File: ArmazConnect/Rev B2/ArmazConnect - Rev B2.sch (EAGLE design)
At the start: 32 parts, among them X0 NC3FAAV2, X1 NC3FAAV2, X2 NC3FAAV2, X3 NC3FAAV2, X4 NC5FAV-SW, X5 NC5MAV-SW, X6 NC5FAV-SW, X8 87832-26

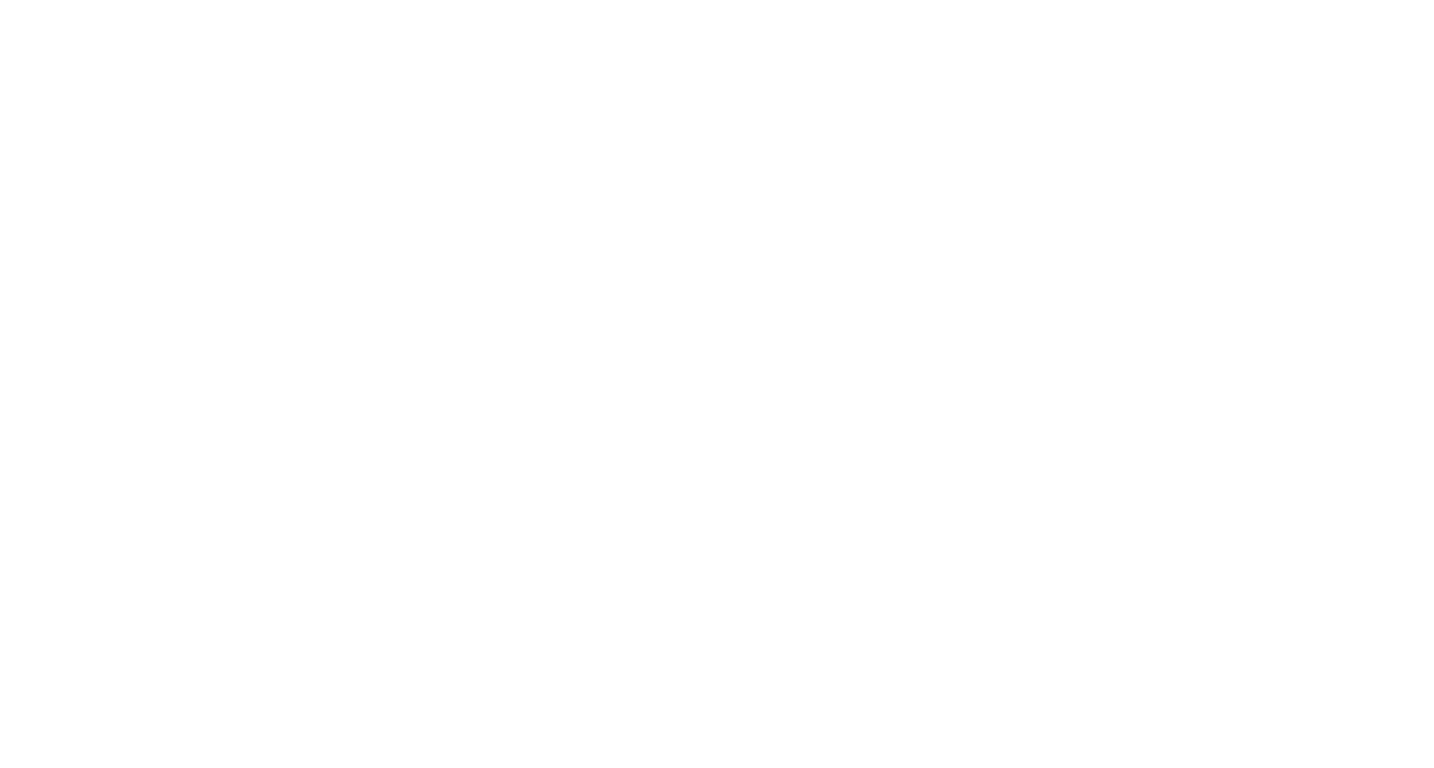
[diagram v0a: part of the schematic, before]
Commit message: Update ArmazConnect - Rev B2 schematic and board, add two dc/dc converter (12V/5V) in parallel
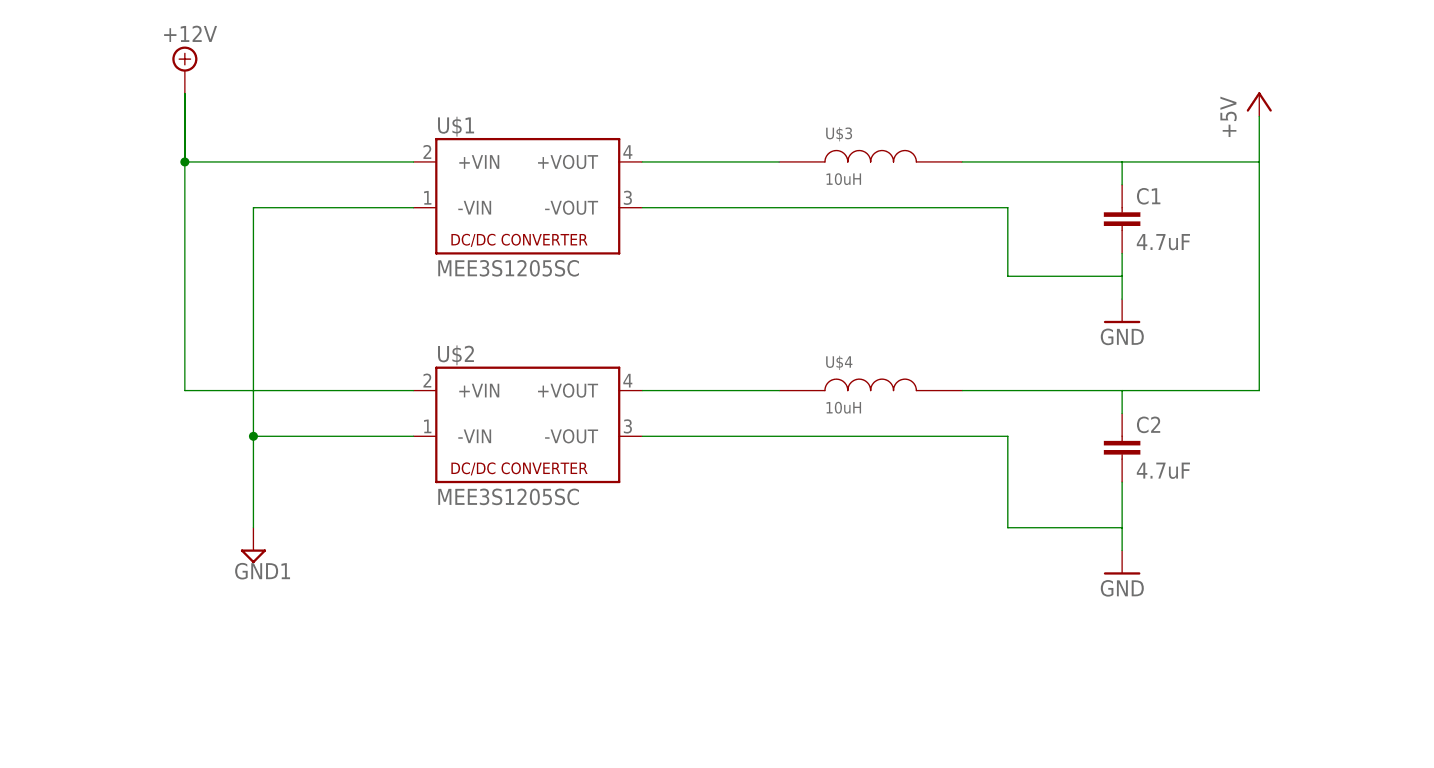
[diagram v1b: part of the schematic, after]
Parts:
- added C1, C2: 4.7uF, rcl:C-EUC0603
- added U$1, U$2: MEE3S1205SC, dc-dc-converter:MEE3S1205SC
- added U$3, U$4: 10uH, murata-inductance:84103C
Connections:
- new net N$5: U$1.+VOUT, U$3.1
- new net N$7: U$2.+VOUT, U$4.1
- net +12V: now also U$1.+VIN, U$2.+VIN
- net +5V: now also C1.1, C2.1, U$3.2, U$4.2
- net GND: now also C1.2, C2.2, U$1.-VOUT, U$2.-VOUT
- net GND1: now also U$1.-VIN, U$2.-VIN
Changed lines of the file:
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@@
 <part name="+3V2" library="supply1" deviceset="+3V3" device=""/>
 <part name="+3V3" library="supply1" deviceset="+3V3" device=""/>
+<part name="U$1" library="dc-dc-converter" deviceset="MEE3" device="" technology="S1205SC"/>
+<part name="U$2" library="dc-dc-converter" deviceset="MEE3" device="" technology="S1205SC"/>
+<part name="P+4" library="supply1" deviceset="+5V" device=""/>
+<part name="GND3" library="supply1" deviceset="GND" device=""/>
+<part name="SUPPLY4" library="supply2" deviceset="+12V" device=""/>
+<part name="SUPPLY5" library="supply2" deviceset="GND1" device=""/>
+<part name="U$3" library="murata-inductance" deviceset="84103C" device="" value="10uH"/>
+<part name="U$4" library="murata-inductance" deviceset="84103C" device="" value="10uH"/>
+<part name="C1" library="rcl" deviceset="C-EU" device="C0603" value="4.7uF"/>
+<part name="C2" library="rcl" deviceset="C-EU" device="C0603" value="4.7uF"/>
+<part name="GND4" library="supply1" deviceset="GND" device=""/>
 </parts>
 <sheets>
@@
 <instance part="+3V2" gate="G$1" x="129.54" y="144.78"/>
 <instance part="+3V3" gate="G$1" x="167.64" y="142.24"/>
+<instance part="U$1" gate="G$1" x="238.76" y="236.22"/>
+<instance part="U$2" gate="G$1" x="238.76" y="210.82"/>
+<instance part="P+4" gate="1" x="320.04" y="246.38"/>
+<instance part="GND3" gate="1" x="304.8" y="193.04" rot="MR0"/>
+<instance part="SUPPLY4" gate="+12V" x="200.66" y="248.92"/>
+<instance part="SUPPLY5" gate="G$1" x="208.28" y="195.58"/>
+<instance part="U$3" gate="L$1" x="276.86" y="238.76"/>
+<instance part="U$4" gate="L$1" x="276.86" y="213.36"/>
+<instance part="C1" gate="G$1" x="304.8" y="233.68"/>
+<instance part="C2" gate="G$1" x="304.8" y="208.28"/>
+<instance part="GND4" gate="1" x="304.8" y="220.98" rot="MR0"/>
 </instances>
 <busses>
@@
 <wire x1="167.64" y1="104.14" x2="167.64" y2="106.68" width="0.1524" layer="91"/>
 </segment>
+<segment>
+<pinref part="C1" gate="G$1" pin="2"/>
+<pinref part="GND4" gate="1" pin="GND"/>
+<wire x1="304.8" y1="223.52" x2="304.8" y2="226.06" width="0.1524" layer="91"/>
+<pinref part="U$1" gate="G$1" pin="-VOUT"/>
+<wire x1="304.8" y1="226.06" x2="304.8" y2="228.6" width="0.1524" layer="91"/>
+<wire x1="251.46" y1="233.68" x2="292.1" y2="233.68" width="0.1524" layer="91"/>
+<wire x1="292.1" y1="226.06" x2="292.1" y2="233.68" width="0.1524" layer="91"/>
+<wire x1="292.1" y1="226.06" x2="304.8" y2="226.06" width="0.1524" layer="91"/>
+</segment>
+<segment>
+<pinref part="GND3" gate="1" pin="GND"/>
+<pinref part="C2" gate="G$1" pin="2"/>
+<wire x1="304.8" y1="195.58" x2="304.8" y2="198.12" width="0.1524" layer="91"/>
+<wire x1="304.8" y1="198.12" x2="304.8" y2="203.2" width="0.1524" layer="91"/>
+<wire x1="304.8" y1="198.12" x2="292.1" y2="198.12" width="0.1524" layer="91"/>
+<wire x1="292.1" y1="198.12" x2="292.1" y2="208.28" width="0.1524" layer="91"/>
+<pinref part="U$2" gate="G$1" pin="-VOUT"/>
+<wire x1="292.1" y1="208.28" x2="251.46" y2="208.28" width="0.1524" layer="91"/>
+</segment>
 </net>
 <net name="N$27" class="0">
@@
 <wire x1="167.64" y1="116.84" x2="167.64" y2="114.3" width="0.1524" layer="91"/>
 </segment>
+<segment>
+<pinref part="U$3" gate="L$1" pin="2"/>
+<wire x1="287.02" y1="238.76" x2="304.8" y2="238.76" width="0.1524" layer="91"/>
+<pinref part="P+4" gate="1" pin="+5V"/>
+<pinref part="U$4" gate="L$1" pin="2"/>
+<wire x1="304.8" y1="238.76" x2="320.04" y2="238.76" width="0.1524" layer="91"/>
+<wire x1="320.04" y1="238.76" x2="320.04" y2="243.84" width="0.1524" layer="91"/>
+<wire x1="287.02" y1="213.36" x2="304.8" y2="213.36" width="0.1524" layer="91"/>
+<wire x1="304.8" y1="213.36" x2="320.04" y2="213.36" width="0.1524" layer="91"/>
+<wire x1="320.04" y1="213.36" x2="320.04" y2="238.76" width="0.1524" layer="91"/>
+<pinref part="C2" gate="G$1" pin="1"/>
+<wire x1="304.8" y1="210.82" x2="304.8" y2="213.36" width="0.1524" layer="91"/>
+<pinref part="C1" gate="G$1" pin="1"/>
+<wire x1="304.8" y1="236.22" x2="304.8" y2="238.76" width="0.1524" layer="91"/>
+</segment>
 </net>
 <net name="ESW0" class="0">
@@
 <junction x="30.48" y="71.12"/>
 </segment>
+<segment>
+<pinref part="U$1" gate="G$1" pin="+VIN"/>
+<pinref part="SUPPLY4" gate="+12V" pin="+12V"/>
+<wire x1="226.06" y1="238.76" x2="200.66" y2="238.76" width="0.1524" layer="91"/>
+<wire x1="200.66" y1="238.76" x2="200.66" y2="246.38" width="0.1524" layer="91"/>
+<pinref part="U$2" gate="G$1" pin="+VIN"/>
+<wire x1="200.66" y1="246.38" x2="200.66" y2="238.76" width="0.1524" layer="91"/>
+<wire x1="200.66" y1="238.76" x2="200.66" y2="213.36" width="0.1524" layer="91"/>
+<wire x1="200.66" y1="213.36" x2="226.06" y2="213.36" width="0.1524" layer="91"/>
+<junction x="200.66" y="238.76"/>
+</segment>
 </net>
 <net name="GND1" class="1">
@@
 <pinref part="SUPPLY12" gate="G$1" pin="GND1"/>
 <wire x1="167.64" y1="127" x2="167.64" y2="129.54" width="0.1524" layer="91"/>
+</segment>
+<segment>
+<pinref part="U$1" gate="G$1" pin="-VIN"/>
+<wire x1="226.06" y1="233.68" x2="208.28" y2="233.68" width="0.1524" layer="91"/>
+<pinref part="SUPPLY5" gate="G$1" pin="GND1"/>
+<wire x1="208.28" y1="233.68" x2="208.28" y2="208.28" width="0.1524" layer="91"/>
+<wire x1="208.28" y1="198.12" x2="208.28" y2="208.28" width="0.1524" layer="91"/>
+<wire x1="208.28" y1="208.28" x2="226.06" y2="208.28" width="0.1524" layer="91"/>
+<pinref part="U$2" gate="G$1" pin="-VIN"/>
+<junction x="208.28" y="208.28"/>
 </segment>
 </net>
@@
 </segment>
 </net>
+<net name="N$5" class="0">
+<segment>
+<pinref part="U$1" gate="G$1" pin="+VOUT"/>
+<pinref part="U$3" gate="L$1" pin="1"/>
+<wire x1="251.46" y1="238.76" x2="266.7" y2="238.76" width="0.1524" layer="91"/>
+</segment>
+</net>
+<net name="N$7" class="0">
+<segment>
+<pinref part="U$4" gate="L$1" pin="1"/>
+<pinref part="U$2" gate="G$1" pin="+VOUT"/>
+<wire x1="266.7" y1="213.36" x2="251.46" y2="213.36" width="0.1524" layer="91"/>
+</segment>
+</net>
 </nets>
 </sheet>
 </sheets>
-<errors>
-</errors>
 </schematic>
 </drawing>

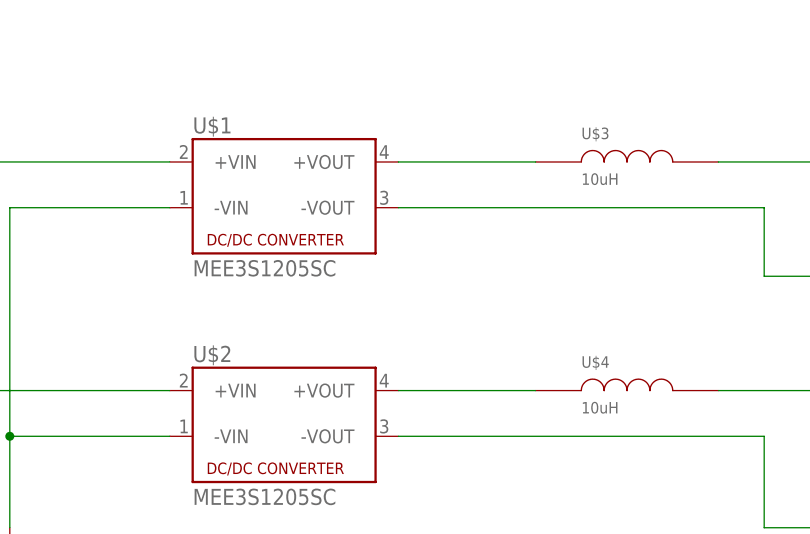
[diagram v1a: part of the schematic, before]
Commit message: Update routing of ArmazConnect- Rev B2 (creation of polygon for +5V and GND1)
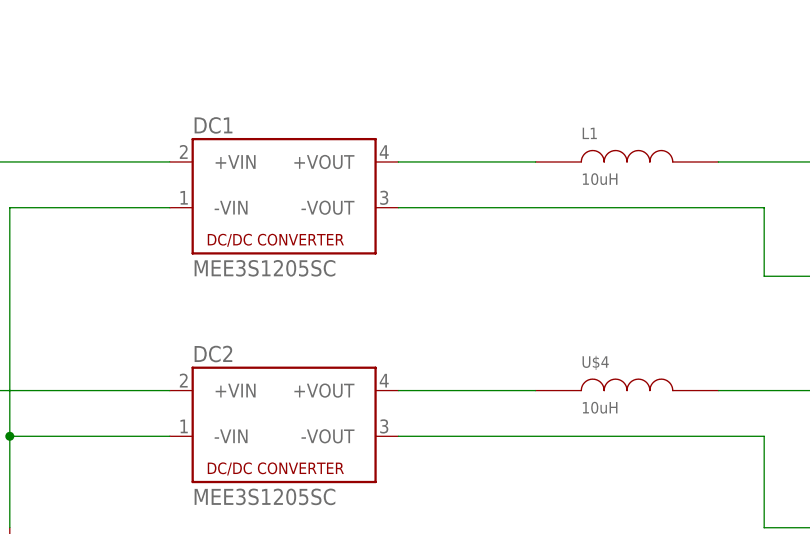
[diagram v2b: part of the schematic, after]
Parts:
- renumbered U$1 to DC1, U$2 to DC2, U$3 to L1
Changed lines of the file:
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@@
 <part name="+3V2" library="supply1" deviceset="+3V3" device=""/>
 <part name="+3V3" library="supply1" deviceset="+3V3" device=""/>
-<part name="U$1" library="dc-dc-converter" deviceset="MEE3" device="" technology="S1205SC"/>
-<part name="U$2" library="dc-dc-converter" deviceset="MEE3" device="" technology="S1205SC"/>
+<part name="DC1" library="dc-dc-converter" deviceset="MEE3" device="" technology="S1205SC"/>
+<part name="DC2" library="dc-dc-converter" deviceset="MEE3" device="" technology="S1205SC"/>
 <part name="P+4" library="supply1" deviceset="+5V" device=""/>
 <part name="GND3" library="supply1" deviceset="GND" device=""/>
 <part name="SUPPLY4" library="supply2" deviceset="+12V" device=""/>
 <part name="SUPPLY5" library="supply2" deviceset="GND1" device=""/>
-<part name="U$3" library="murata-inductance" deviceset="84103C" device="" value="10uH"/>
+<part name="L1" library="murata-inductance" deviceset="84103C" device="" value="10uH"/>
 <part name="U$4" library="murata-inductance" deviceset="84103C" device="" value="10uH"/>
 <part name="C1" library="rcl" deviceset="C-EU" device="C0603" value="4.7uF"/>
@@
 <instance part="+3V2" gate="G$1" x="129.54" y="144.78"/>
 <instance part="+3V3" gate="G$1" x="167.64" y="142.24"/>
-<instance part="U$1" gate="G$1" x="238.76" y="236.22"/>
-<instance part="U$2" gate="G$1" x="238.76" y="210.82"/>
+<instance part="DC1" gate="G$1" x="238.76" y="236.22"/>
+<instance part="DC2" gate="G$1" x="238.76" y="210.82"/>
 <instance part="P+4" gate="1" x="320.04" y="246.38"/>
 <instance part="GND3" gate="1" x="304.8" y="193.04" rot="MR0"/>
 <instance part="SUPPLY4" gate="+12V" x="200.66" y="248.92"/>
 <instance part="SUPPLY5" gate="G$1" x="208.28" y="195.58"/>
-<instance part="U$3" gate="L$1" x="276.86" y="238.76"/>
+<instance part="L1" gate="L$1" x="276.86" y="238.76"/>
 <instance part="U$4" gate="L$1" x="276.86" y="213.36"/>
 <instance part="C1" gate="G$1" x="304.8" y="233.68"/>
@@
 <pinref part="GND4" gate="1" pin="GND"/>
 <wire x1="304.8" y1="223.52" x2="304.8" y2="226.06" width="0.1524" layer="91"/>
-<pinref part="U$1" gate="G$1" pin="-VOUT"/>
+<pinref part="DC1" gate="G$1" pin="-VOUT"/>
 <wire x1="304.8" y1="226.06" x2="304.8" y2="228.6" width="0.1524" layer="91"/>
 <wire x1="251.46" y1="233.68" x2="292.1" y2="233.68" width="0.1524" layer="91"/>
@@
 <wire x1="304.8" y1="198.12" x2="292.1" y2="198.12" width="0.1524" layer="91"/>
 <wire x1="292.1" y1="198.12" x2="292.1" y2="208.28" width="0.1524" layer="91"/>
-<pinref part="U$2" gate="G$1" pin="-VOUT"/>
+<pinref part="DC2" gate="G$1" pin="-VOUT"/>
 <wire x1="292.1" y1="208.28" x2="251.46" y2="208.28" width="0.1524" layer="91"/>
 </segment>
@@
 </segment>
 <segment>
-<pinref part="U$3" gate="L$1" pin="2"/>
+<pinref part="L1" gate="L$1" pin="2"/>
 <wire x1="287.02" y1="238.76" x2="304.8" y2="238.76" width="0.1524" layer="91"/>
 <pinref part="P+4" gate="1" pin="+5V"/>
@@
 </segment>
 <segment>
-<pinref part="U$1" gate="G$1" pin="+VIN"/>
+<pinref part="DC1" gate="G$1" pin="+VIN"/>
 <pinref part="SUPPLY4" gate="+12V" pin="+12V"/>
 <wire x1="226.06" y1="238.76" x2="200.66" y2="238.76" width="0.1524" layer="91"/>
 <wire x1="200.66" y1="238.76" x2="200.66" y2="246.38" width="0.1524" layer="91"/>
-<pinref part="U$2" gate="G$1" pin="+VIN"/>
+<pinref part="DC2" gate="G$1" pin="+VIN"/>
 <wire x1="200.66" y1="246.38" x2="200.66" y2="238.76" width="0.1524" layer="91"/>
 <wire x1="200.66" y1="238.76" x2="200.66" y2="213.36" width="0.1524" layer="91"/>
@@
 </segment>
 <segment>
-<pinref part="U$1" gate="G$1" pin="-VIN"/>
+<pinref part="DC1" gate="G$1" pin="-VIN"/>
 <wire x1="226.06" y1="233.68" x2="208.28" y2="233.68" width="0.1524" layer="91"/>
 <pinref part="SUPPLY5" gate="G$1" pin="GND1"/>
@@
 <wire x1="208.28" y1="198.12" x2="208.28" y2="208.28" width="0.1524" layer="91"/>
 <wire x1="208.28" y1="208.28" x2="226.06" y2="208.28" width="0.1524" layer="91"/>
-<pinref part="U$2" gate="G$1" pin="-VIN"/>
+<pinref part="DC2" gate="G$1" pin="-VIN"/>
 <junction x="208.28" y="208.28"/>
 </segment>
@@
 <net name="N$5" class="0">
 <segment>
-<pinref part="U$1" gate="G$1" pin="+VOUT"/>
-<pinref part="U$3" gate="L$1" pin="1"/>
+<pinref part="DC1" gate="G$1" pin="+VOUT"/>
+<pinref part="L1" gate="L$1" pin="1"/>
 <wire x1="251.46" y1="238.76" x2="266.7" y2="238.76" width="0.1524" layer="91"/>
 </segment>
@@
 <segment>
 <pinref part="U$4" gate="L$1" pin="1"/>
-<pinref part="U$2" gate="G$1" pin="+VOUT"/>
+<pinref part="DC2" gate="G$1" pin="+VOUT"/>
 <wire x1="266.7" y1="213.36" x2="251.46" y2="213.36" width="0.1524" layer="91"/>
 </segment>
